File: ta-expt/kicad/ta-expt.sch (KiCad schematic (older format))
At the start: 34 parts, among them IC1 STM32L496RGT3, IC2 IS25LP128F-JBLA3, J1 Conn_01x16, J2 Conn_01x16, J3 Conn_01x04, J4 Conn_02x06_Odd_Even, J5 Conn_01x04, Q1 FDY300NZ, Q2 FDY300NZ, Y1 ABM8AIG-16.000MHZ-12-2Z-T, Y2 ABS07AIG-32.768kHz-T

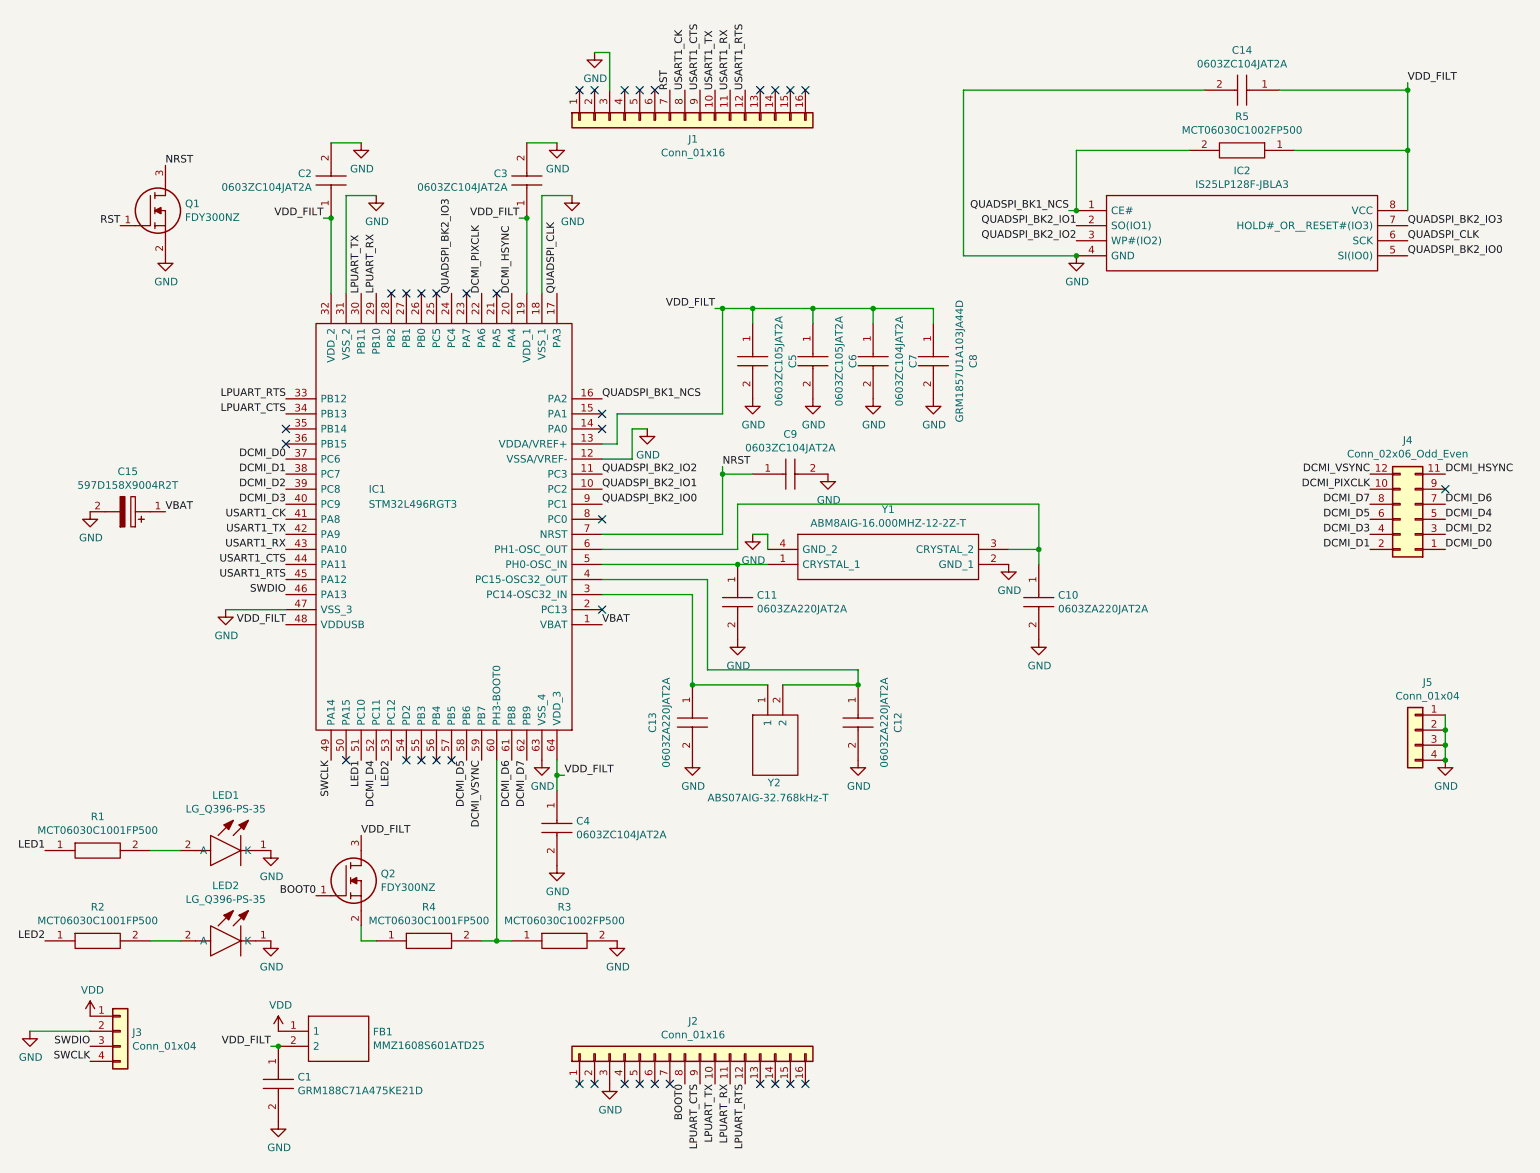
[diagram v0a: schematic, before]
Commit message: Tartan Artibeus experiment board v1.0.0
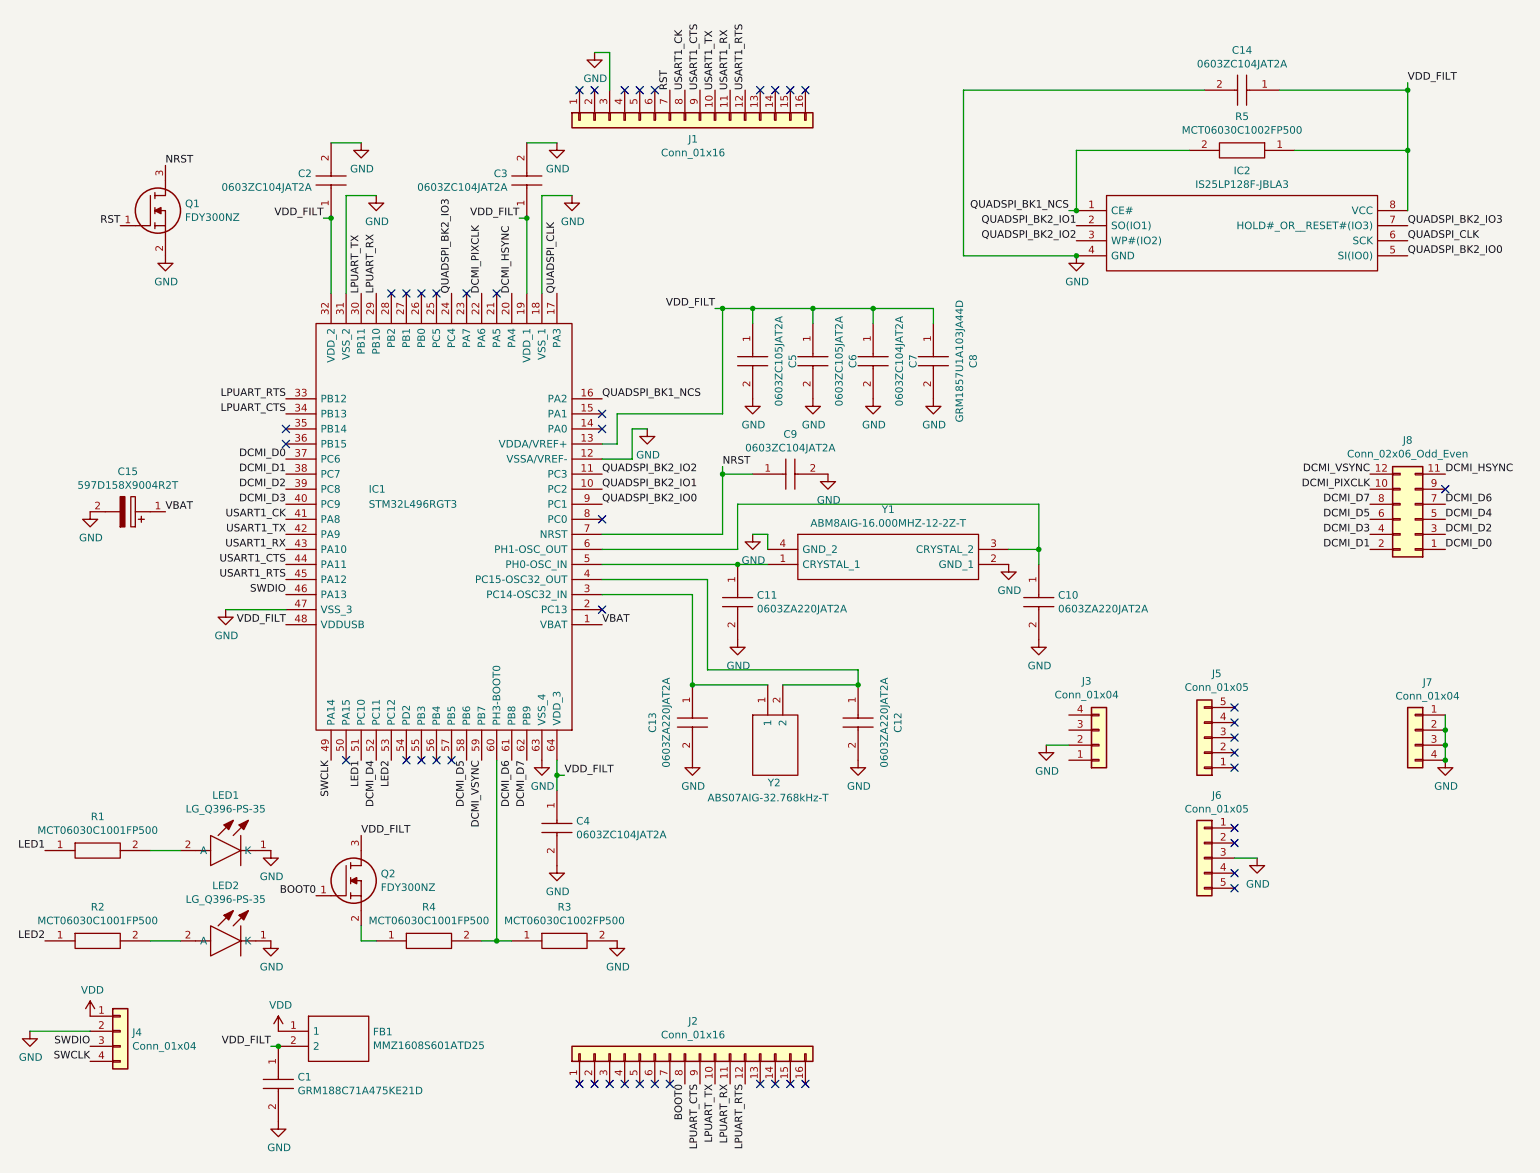
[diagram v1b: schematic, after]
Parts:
- added J3: Conn_01x04, ta-expt:PinSocket_4x1_TartanArtibeus, symbol Connector_Generic:Conn_01x04
- added J5, J6: Conn_01x05, ta-expt:PinSocket_1x5_TartanArtibeus, symbol Connector_Generic:Conn_01x05
- renumbered J3 to J4, J5 to J7, J4 to J8
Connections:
- net GND: now also J3.2 (Pin_2), J6.3 (Pin_3); no longer J2.3 (Pin_3)
- no-connect marks 37 -> 47
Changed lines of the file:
@@
 NoConn ~ 4250 7550
 $Comp
-L Connector_Generic:Conn_02x06_Odd_Even J4
+L Connector_Generic:Conn_02x06_Odd_Even J8
 U 1 1 5F1C48F2
 P 9800 3800
-F 0 "J4" H 9850 3275 50  0000 C CNN
+F 0 "J8" H 9850 3275 50  0000 C CNN
 F 1 "Conn_02x06_Odd_Even" H 9850 3366 50  0000 C CNN
 F 2 "ta-expt:PinSocket_6x2_TartanArtibeus" H 9800 3800 50  0001 C CNN
@@
 $EndComp
 $Comp
-L Connector_Generic:Conn_01x04 J3
+L Connector_Generic:Conn_01x04 J4
 U 1 1 5F20BEB9
 P 1200 7200
-F 0 "J3" H 1280 7192 50  0000 L CNN
+F 0 "J4" H 1280 7192 50  0000 L CNN
 F 1 "Conn_01x04" H 1280 7101 50  0000 L CNN
 F 2 "ta-expt:PinSocket_4x1_TartanArtibeus" H 1200 7200 50  0001 C CNN
@@
 Connection ~ 9750 1350
 $Comp
-L Connector_Generic:Conn_01x04 J5
+L Connector_Generic:Conn_01x04 J7
 U 1 1 5F269F00
 P 9800 5200
-F 0 "J5" H 9718 5517 50  0000 C CNN
+F 0 "J7" H 9718 5517 50  0000 C CNN
 F 1 "Conn_01x04" H 9718 5426 50  0000 C CNN
 F 2 "ta-expt:MountingHoles_TartanArtibeus" H 9800 5200 50  0001 C CNN
@@
 $EndComp
 $Comp
-L power:GND #PWR?
+L power:GND #PWR031
 U 1 1 5F199C49
 P 4350 700
-F 0 "#PWR?" H 4350 450 50  0001 C CNN
+F 0 "#PWR031" H 4350 450 50  0001 C CNN
 F 1 "GND" H 4355 527 50  0000 C CNN
 F 2 "" H 4350 700 50  0001 C CNN
@@
 	4450 700  4350 700
 $Comp
-L power:GND #PWR?
-U 1 1 5F1A332F
-P 4450 7550
-F 0 "#PWR?" H 4450 7300 50  0001 C CNN
-F 1 "GND" H 4455 7377 50  0000 C CNN
-F 2 "" H 4450 7550 50  0001 C CNN
-F 3 "" H 4450 7550 50  0001 C CNN
-	1    4450 7550
-	1    0    0    -1
-$EndComp
+L Connector_Generic:Conn_01x04 J3
+U 1 1 5F2138DD
+P 7700 5300
+F 0 "J3" H 7618 4875 50  0000 C CNN
+F 1 "Conn_01x04" H 7618 4966 50  0000 C CNN
+F 2 "ta-expt:PinSocket_4x1_TartanArtibeus" H 7700 5300 50  0001 C CNN
+F 3 "~" H 7700 5300 50  0001 C CNN
+	1    7700 5300
+	1    0    0    1
+$EndComp
+$Comp
+L Connector_Generic:Conn_01x05 J6
+U 1 1 5F217B40
+P 8400 6050
+F 0 "J6" H 8318 6467 50  0000 C CNN
+F 1 "Conn_01x05" H 8318 6376 50  0000 C CNN
+F 2 "ta-expt:PinSocket_1x5_TartanArtibeus" H 8400 6050 50  0001 C CNN
+F 3 "~" H 8400 6050 50  0001 C CNN
+	1    8400 6050
+	-1   0    0    -1
+$EndComp
+$Comp
+L Connector_Generic:Conn_01x05 J5
+U 1 1 5F2152E2
+P 8400 5250
+F 0 "J5" H 8318 4825 50  0000 C CNN
+F 1 "Conn_01x05" H 8318 4916 50  0000 C CNN
+F 2 "ta-expt:PinSocket_1x5_TartanArtibeus" H 8400 5250 50  0001 C CNN
+F 3 "~" H 8400 5250 50  0001 C CNN
+	1    8400 5250
+	-1   0    0    1
+$EndComp
+$Comp
+L power:GND #PWR032
+U 1 1 5F222EE1
+P 7350 5300
+F 0 "#PWR032" H 7350 5050 50  0001 C CNN
+F 1 "GND" H 7355 5127 50  0000 C CNN
+F 2 "" H 7350 5300 50  0001 C CNN
+F 3 "" H 7350 5300 50  0001 C CNN
+	1    7350 5300
+	1    0    0    -1
+$EndComp
+Wire Wire Line
+	7500 5300 7350 5300
+NoConn ~ 8600 5050
+NoConn ~ 8600 5150
+NoConn ~ 8600 5250
+NoConn ~ 8600 5350
+NoConn ~ 8600 5450
+$Comp
+L power:GND #PWR033
+U 1 1 5F22D3EC
+P 8750 6050
+F 0 "#PWR033" H 8750 5800 50  0001 C CNN
+F 1 "GND" H 8755 5877 50  0000 C CNN
+F 2 "" H 8750 6050 50  0001 C CNN
+F 3 "" H 8750 6050 50  0001 C CNN
+	1    8750 6050
+	1    0    0    -1
+$EndComp
+NoConn ~ 8600 5850
+NoConn ~ 8600 5950
+NoConn ~ 8600 6150
+NoConn ~ 8600 6250
+Wire Wire Line
+	8750 6050 8600 6050
+NoConn ~ 4450 7550
 $EndSCHEMATC

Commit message: Tartan Artibeus experiment board v1.0.1
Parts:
- removed Q1, Q2: FDY300NZ, ta-expt:SOTFL50P160X78-3N, symbol ta-expt:FDY300NZ
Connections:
- net RST is gone; now on net NRST: J1.7 (Pin_7)
- net BOOT0: now also R4.1
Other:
- note added: "(Internally pulled up)"
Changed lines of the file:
@@
 VDD_FILT
-$Comp
-L ta-expt:FDY300NZ Q2
-U 1 1 5F096B89
-P 2500 6300
-F 0 "Q2" H 2930 6446 50  0000 L CNN
-F 1 "FDY300NZ" H 2930 6355 50  0000 L CNN
-F 2 "ta-expt:SOTFL50P160X78-3N" H 2950 6250 50  0001 L CNN
-F 3 "https://www.onsemi.com/pub/Collateral/FDY300NZ-D.pdf" H 2950 6150 50  0001 L CNN
-F 4 "Trans MOSFET N-CH 20V 0.6A 3-Pin SC-89" H 2950 6050 50  0001 L CNN "Description"
-F 5 "0.78" H 2950 5950 50  0001 L CNN "Height"
-F 6 "ON Semiconductor" H 2950 5850 50  0001 L CNN "Manufacturer_Name"
-F 7 "FDY300NZ" H 2950 5750 50  0001 L CNN "Manufacturer_Part_Number"
-F 8 "FDY300NZ" H 2950 5650 50  0001 L CNN "Arrow Part Number"
-F 9 "https://www.arrow.com/en/products/fdy300nz/on-semiconductor" H 2950 5550 50  0001 L CNN "Arrow Price/Stock"
-F 10 "512-FDY300NZ" H 2950 5450 50  0001 L CNN "Mouser Part Number"
-F 11 "https://www.mouser.co.uk/ProductDetail/ON-Semiconductor-Fairchild/FDY300NZ?qs=QGk6feVlqMK1iUZo3Em7Lw%3D%3D" H 2950 5350 50  0001 L CNN "Mouser Price/Stock"
-	1    2500 6300
-	1    0    0    -1
-$EndComp
 $Comp
 L ta-expt:MCT06030C1002FP500 R3
@@
 Connection ~ 3700 6600
 Wire Wire Line
-	2800 6500 2800 6600
-Wire Wire Line
 	2800 6600 2900 6600
-Text Label 2800 5900 0    50   ~ 0
-VDD_FILT
-Text Label 2500 6300 2    50   ~ 0
+Text Label 2800 6600 2    50   ~ 0
 BOOT0
 $Comp
@@
 USART1_CK
 Text Label 4850 950  1    50   ~ 0
-RST
+NRST
 NoConn ~ 5750 950
 NoConn ~ 5650 950
@@
 Text Label 2200 7300 2    50   ~ 0
 VDD_FILT
-$Comp
-L ta-expt:FDY300NZ Q1
-U 1 1 5F22AD93
-P 1200 1850
-F 0 "Q1" H 1630 1996 50  0000 L CNN
-F 1 "FDY300NZ" H 1630 1905 50  0000 L CNN
-F 2 "ta-expt:SOTFL50P160X78-3N" H 1650 1800 50  0001 L CNN
-F 3 "https://www.onsemi.com/pub/Collateral/FDY300NZ-D.pdf" H 1650 1700 50  0001 L CNN
-F 4 "Trans MOSFET N-CH 20V 0.6A 3-Pin SC-89" H 1650 1600 50  0001 L CNN "Description"
-F 5 "0.78" H 1650 1500 50  0001 L CNN "Height"
-F 6 "ON Semiconductor" H 1650 1400 50  0001 L CNN "Manufacturer_Name"
-F 7 "FDY300NZ" H 1650 1300 50  0001 L CNN "Manufacturer_Part_Number"
-F 8 "FDY300NZ" H 1650 1200 50  0001 L CNN "Arrow Part Number"
-F 9 "https://www.arrow.com/en/products/fdy300nz/on-semiconductor" H 1650 1100 50  0001 L CNN "Arrow Price/Stock"
-F 10 "512-FDY300NZ" H 1650 1000 50  0001 L CNN "Mouser Part Number"
-F 11 "https://www.mouser.co.uk/ProductDetail/ON-Semiconductor-Fairchild/FDY300NZ?qs=QGk6feVlqMK1iUZo3Em7Lw%3D%3D" H 1650 900 50  0001 L CNN "Mouser Price/Stock"
-	1    1200 1850
-	1    0    0    -1
-$EndComp
-Text Label 1500 1450 0    50   ~ 0
-NRST
-$Comp
-L power:GND #PWR04
-U 1 1 5F22E989
-P 1500 2050
-F 0 "#PWR04" H 1500 1800 50  0001 C CNN
-F 1 "GND" H 1505 1877 50  0000 C CNN
-F 2 "" H 1500 2050 50  0001 C CNN
-F 3 "" H 1500 2050 50  0001 C CNN
-	1    1500 2050
-	1    0    0    -1
-$EndComp
-Text Label 1200 1850 2    50   ~ 0
-RST
 Wire Wire Line
 	9750 1750 9750 1350
@@
 	8750 6050 8600 6050
 NoConn ~ 4450 7550
+Text Notes 3150 3900 0    50   ~ 0
+(Internally pulled up)
 $EndSCHEMATC
